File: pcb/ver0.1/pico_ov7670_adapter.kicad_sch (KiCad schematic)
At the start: 19 parts, among them J1 GPIO Header, SW1 SW_Push, SW2 SW_Push, U1 CAMERA-OV7670, U2 RASPBERRY_PI_PICO_W

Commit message: basic rotuing completed
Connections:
- net PICO_IO16: now also J1.10 (Pin_10); no longer J1.4 (Pin_4)
- net PICO_IO17: now also J1.9 (Pin_9); no longer J1.6 (Pin_6)
- net PICO_IO20: now also J1.6 (Pin_6); no longer J1.5 (Pin_5)
- net PICO_IO22: now also J1.4 (Pin_4); no longer J1.8 (Pin_8)
- net USER_Button: now also U2.31 (I2C1_SDA/ADC0/GP26); no longer U2.24 (I2C1_SDA/SPI0_SCK/GP18)
- net USER_LED: now also U2.34 (ADC2_GP28); no longer U2.25 (I2C1_SCL/SPI0_TX/GP19)
- net at R2.2: now also U2.7 (UART1_RX/I2C0_SCL/SPI0_CSN/GP5); no longer U2.16 (UART0_TX/I2C0_SDA/SPI1_RX/GP12)
- net at R6.2: now also U2.6 (UART1_TX/I2C0_SDA/SPI0_RX/GP4); no longer U2.17 (UART0_RX/I2C0_SCL/SPI1_CSN/GP13)
- net PICO_IO21: now reaches U2.27 (12C0_SCL/GP21)
- net PICO_IO21: now also J1.5 (Pin_5)
- net OV_D0_PICO_IO0 renamed OV_D0_PICO_IO14
- net OV_D0_PICO_IO14: now also U2.17 (UART0_RX/I2C0_SCL/SPI1_CSN/GP13); no longer U2.1 (UART0_TX/I2C0_SDA/SPI0_RX/GP0)
- net OV_D1_PICO_IO1 renamed OV_D1_PICO_IO13
- net OV_D1_PICO_IO13: now also U2.16 (UART0_TX/I2C0_SDA/SPI1_RX/GP12); no longer U2.2 (UART0_RX/I2C0_SCL/SPI0_CSN/GP1)
- net OV_D2_PICO_IO2 renamed OV_D2_PICO_IO12
- net OV_D2_PICO_IO12: now also U2.15 (I2C1_SCL/SPI1_TX/GP11); no longer U2.4 (I2C1_SDA/SPI0_SCK/GP2)
- net OV_D3_PICO_IO3 renamed OV_D3_PICO_IO10
- net OV_D3_PICO_IO10: now also U2.14 (I2C1_SDA/SPI1_SCK/GP10); no longer U2.5 (I2C1_SCL/SPI0_TX/GP3)
- net OV_D4_PICO_IO4 renamed OV_D4_PICO_IO9
- net OV_D4_PICO_IO9: now also U2.12 (UART1_RX/I2C0_SCL/SPI1_CSN/GP9); no longer U2.6 (UART1_TX/I2C0_SDA/SPI0_RX/GP4)
- net OV_D5_PICO_IO5 renamed OV_D5_PICO_IO8
- net OV_D5_PICO_IO8: now also U2.11 (UART1_TX/I2C0_SDA/SPI1_RX/GP8); no longer U2.7 (UART1_RX/I2C0_SCL/SPI0_CSN/GP5)
- net OV_D6_PICO_IO6 renamed OV_D6_PICO_IO7
- net OV_D6_PICO_IO7: now also U2.10 (I2C1_SCL/SPI0_TX/GP7); no longer U2.9 (I2C1_SDA/SPI0_SCK/GP6)
- net OV_D7_PICO_IO7 renamed OV_D7_PICO_IO6
- net OV_D7_PICO_IO6: now also U2.9 (I2C1_SDA/SPI0_SCK/GP6); no longer U2.10 (I2C1_SCL/SPI0_TX/GP7)
- net OV_HREF_PICO_IO11 renamed OV_HREF_PICO_IO3
- net OV_HREF_PICO_IO3: now also U2.5 (I2C1_SCL/SPI0_TX/GP3); no longer U2.14 (I2C1_SDA/SPI1_SCK/GP10)
- net OV_PCLK_PICO_IO9 renamed OV_PCLK_PICO_IO4
- net OV_SCL_PICO_IO13_SCL renamed OV_SCL_PICO_IO1_SCL
- net OV_SCL_PICO_IO1_SCL: now also U2.2 (UART0_RX/I2C0_SCL/SPI0_CSN/GP1); no longer U2.12 (UART1_RX/I2C0_SCL/SPI1_CSN/GP9)
- net OV_SDA_PICO_IO12_SDA renamed OV_SDA_PICO_IO0_SDA
- net OV_SDA_PICO_IO0_SDA: now also U2.1 (UART0_TX/I2C0_SDA/SPI0_RX/GP0); no longer U2.11 (UART1_TX/I2C0_SDA/SPI1_RX/GP8)
- net OV_VSYNC_PICO_IO10 renamed OV_VSYNC_PICO_IO2
- net OV_VSYNC_PICO_IO2: now also U2.4 (I2C1_SDA/SPI0_SCK/GP2); no longer U2.15 (I2C1_SCL/SPI1_TX/GP11)
- net OV_XCLK_PICO_IO8 renamed OV_XCLK_PICO_IO5
- net PICO_IO26 renamed PICO_IO19
- net PICO_IO19: now also U2.25 (I2C1_SCL/SPI0_TX/GP19); no longer U2.31 (I2C1_SDA/ADC0/GP26)
- net PICO_IO27: no longer names the net of U2.32 (I2C1_SCL/ADC1/GP27)
- net PICO_IO27: no longer J1.10 (Pin_10)
- removed net PICO_IO28: J1.9 (Pin_9), U2.34 (ADC2_GP28)
- new net PICO_IO18: J1.8 (Pin_8), U2.24 (I2C1_SDA/SPI0_SCK/GP18)
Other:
- moved on the sheet: R2, R6

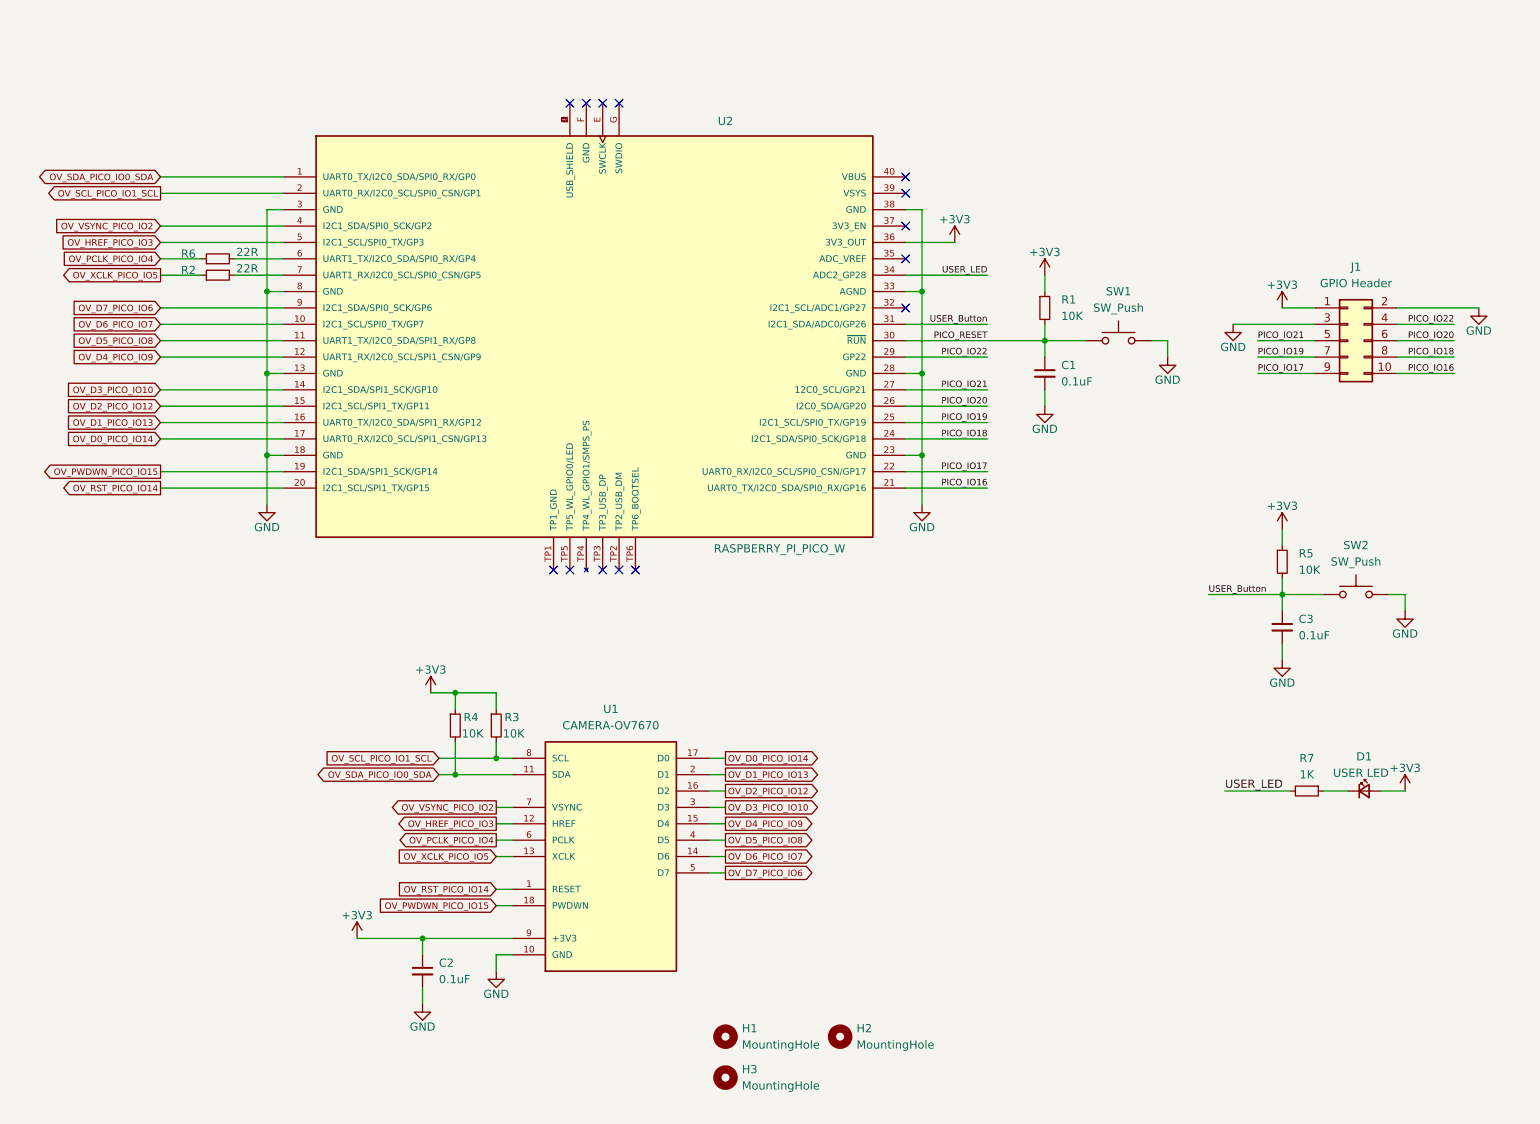
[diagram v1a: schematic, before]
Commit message: GPIO header change updated
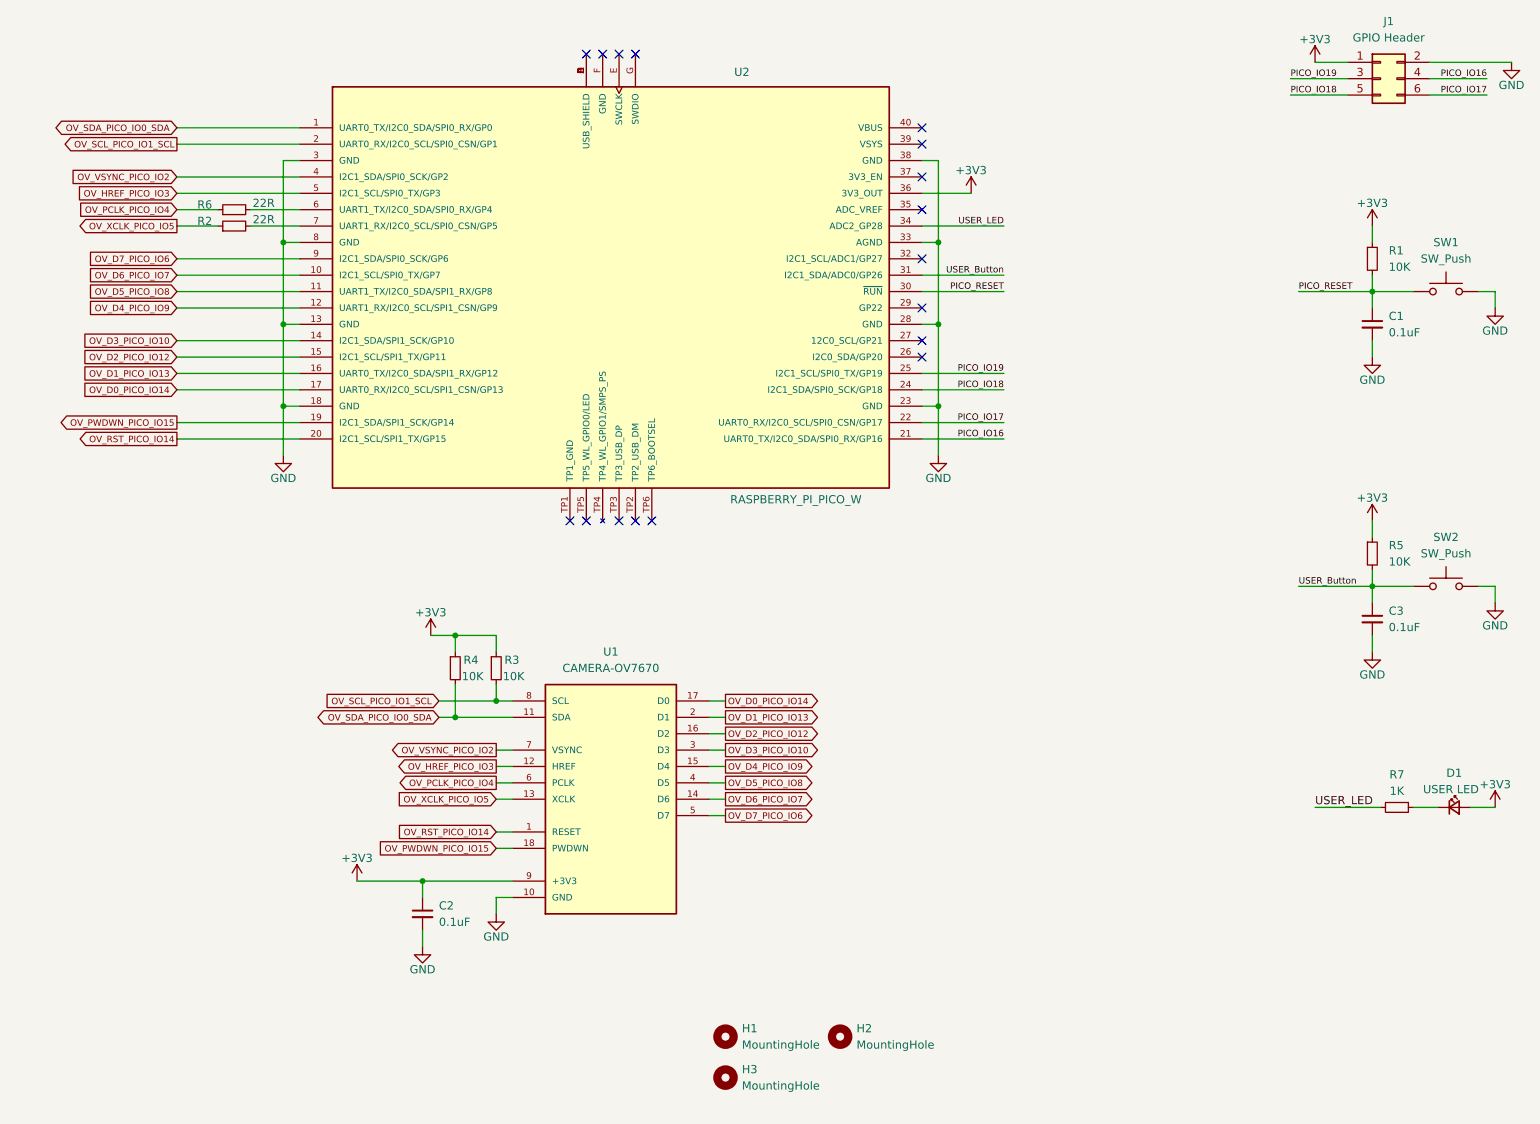
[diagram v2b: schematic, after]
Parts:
- removed J1: GPIO Header, Connector_PinHeader_2.54mm:PinHeader_2x05_P2.54mm_Vertical, symbol Connector_Generic:Conn_02x05_Odd_Even
- added J1: GPIO Header, Connector_PinHeader_2.54mm:PinHeader_2x03_P2.54mm_Vertical, symbol Connector_Generic:Conn_02x03_Odd_Even
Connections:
- net +3V3: now also J1.1 (Pin_1)
- net GND: now also J1.2 (Pin_2)
- net PICO_IO16: now also J1.4 (Pin_4)
- net PICO_IO17: now also J1.6 (Pin_6)
- net PICO_IO18: now also J1.5 (Pin_5)
- net PICO_IO19: now also J1.3 (Pin_3)
- net PICO_IO20: no longer names the net of U2.26 (I2C0_SDA/GP20)
- net PICO_IO21: no longer names the net of U2.27 (12C0_SCL/GP21)
- net PICO_IO22: no longer names the net of U2.29 (GP22)
- no-connect marks 14 -> 17
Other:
- moved on the sheet: C1, C2, C3, D1, R1, R2, R3, R4, R5, R6, R7, SW1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

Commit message: gerber files added
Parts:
- added FID1, FID2, FID3: Fiducial, Fiducial:Fiducial_0.5mm_Mask1mm, symbol Mechanical:Fiducial
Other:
- moved on the sheet: H1, H2, H3
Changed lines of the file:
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@@
 	(symbol
 		(lib_id "Mechanical:MountingHole")
-		(at 139.7 184.15 0)
+		(at 139.7 186.69 0)
 		(unit 1)
 		(exclude_from_sim yes)
@@
 		(fields_autoplaced yes)
 		(property "Reference" "H1"
-			(at 142.24 182.8799 0)
+			(at 142.24 185.4199 0)
 			(effects
 				(font
@@
 		)
 		(property "Value" "MountingHole"
-			(at 142.24 185.4199 0)
+			(at 142.24 187.9599 0)
 			(effects
 				(font
@@
 		)
 		(property "Footprint" "MountingHole:MountingHole_3.2mm_M3_DIN965"
-			(at 139.7 184.15 0)
+			(at 139.7 186.69 0)
 			(effects
 				(font
@@
 		)
 		(property "Datasheet" "~"
-			(at 139.7 184.15 0)
+			(at 139.7 186.69 0)
 			(effects
 				(font
@@
 		)
 		(property "Description" "Mounting Hole without connection"
-			(at 139.7 184.15 0)
+			(at 139.7 186.69 0)
 			(effects
 				(font
@@
 	(symbol
 		(lib_id "Mechanical:MountingHole")
-		(at 139.7 190.5 0)
+		(at 139.7 193.04 0)
 		(unit 1)
 		(exclude_from_sim yes)
@@
 		(fields_autoplaced yes)
 		(property "Reference" "H3"
-			(at 142.24 189.2299 0)
+			(at 142.24 191.7699 0)
 			(effects
 				(font
@@
 		)
 		(property "Value" "MountingHole"
-			(at 142.24 191.7699 0)
+			(at 142.24 194.3099 0)
 			(effects
 				(font
@@
 		)
 		(property "Footprint" "MountingHole:MountingHole_3.2mm_M3_DIN965"
-			(at 139.7 190.5 0)
+			(at 139.7 193.04 0)
 			(effects
 				(font
@@
 		)
 		(property "Datasheet" "~"
-			(at 139.7 190.5 0)
+			(at 139.7 193.04 0)
 			(effects
 				(font
@@
 		)
 		(property "Description" "Mounting Hole without connection"
-			(at 139.7 190.5 0)
+			(at 139.7 193.04 0)
 			(effects
 				(font
@@
 	)
 	(symbol
+		(lib_id "Mechanical:Fiducial")
+		(at 124.46 186.69 0)
+		(unit 1)
+		(exclude_from_sim yes)
+		(in_bom no)
+		(on_board yes)
+		(dnp no)
+		(property "Reference" "FID3"
+			(at 122.174 183.896 0)
+			(effects
+				(font
+					(size 1.27 1.27)
+				)
+				(justify left)
+			)
+		)
+		(property "Value" "Fiducial"
+			(at 127 187.9599 0)
+			(effects
+				(font
+					(size 1.27 1.27)
+				)
+				(justify left)
+				(hide yes)
+			)
+		)
+		(property "Footprint" "Fiducial:Fiducial_0.5mm_Mask1mm"
+			(at 124.46 186.69 0)
+			(effects
+				(font
+					(size 1.27 1.27)
+				)
+				(hide yes)
+			)
+		)
+		(property "Datasheet" "~"
+			(at 124.46 186.69 0)
+			(effects
+				(font
+					(size 1.27 1.27)
+				)
+				(hide yes)
+			)
+		)
+		(property "Description" "Fiducial Marker"
+			(at 124.46 186.69 0)
+			(effects
+				(font
+					(size 1.27 1.27)
+				)
+				(hide yes)
+			)
+		)
+		(instances
+			(project "pico_ov7670_adapter"
+				(path "/8ca4dbff-a6fb-40ff-ba8a-6032e61c2093"
+					(reference "FID3")
+					(unit 1)
+				)
+			)
+		)
+	)
+	(symbol
 		(lib_id "Device:R_Small")
 		(at 240.03 109.22 0)
@@
 	(symbol
 		(lib_id "Mechanical:MountingHole")
-		(at 157.48 184.15 0)
+		(at 157.48 186.69 0)
 		(unit 1)
 		(exclude_from_sim yes)
@@
 		(fields_autoplaced yes)
 		(property "Reference" "H2"
-			(at 160.02 182.8799 0)
+			(at 160.02 185.4199 0)
 			(effects
 				(font
@@
 		)
 		(property "Value" "MountingHole"
-			(at 160.02 185.4199 0)
+			(at 160.02 187.9599 0)
 			(effects
 				(font
@@
 		)
 		(property "Footprint" "MountingHole:MountingHole_3.2mm_M3_DIN965"
-			(at 157.48 184.15 0)
+			(at 157.48 186.69 0)
 			(effects
 				(font
@@
 		)
 		(property "Datasheet" "~"
-			(at 157.48 184.15 0)
+			(at 157.48 186.69 0)
 			(effects
 				(font
@@
 		)
 		(property "Description" "Mounting Hole without connection"
-			(at 157.48 184.15 0)
+			(at 157.48 186.69 0)
 			(effects
 				(font
@@
 	)
 	(symbol
+		(lib_id "Mechanical:Fiducial")
+		(at 116.84 186.69 0)
+		(unit 1)
+		(exclude_from_sim yes)
+		(in_bom no)
+		(on_board yes)
+		(dnp no)
+		(property "Reference" "FID2"
+			(at 114.554 183.896 0)
+			(effects
+				(font
+					(size 1.27 1.27)
+				)
+				(justify left)
+			)
+		)
+		(property "Value" "Fiducial"
+			(at 119.38 187.9599 0)
+			(effects
+				(font
+					(size 1.27 1.27)
+				)
+				(justify left)
+				(hide yes)
+			)
+		)
+		(property "Footprint" "Fiducial:Fiducial_0.5mm_Mask1mm"
+			(at 116.84 186.69 0)
+			(effects
+				(font
+					(size 1.27 1.27)
+				)
+				(hide yes)
+			)
+		)
+		(property "Datasheet" "~"
+			(at 116.84 186.69 0)
+			(effects
+				(font
+					(size 1.27 1.27)
+				)
+				(hide yes)
+			)
+		)
+		(property "Description" "Fiducial Marker"
+			(at 116.84 186.69 0)
+			(effects
+				(font
+					(size 1.27 1.27)
+				)
+				(hide yes)
+			)
+		)
+		(instances
+			(project "pico_ov7670_adapter"
+				(path "/8ca4dbff-a6fb-40ff-ba8a-6032e61c2093"
+					(reference "FID2")
+					(unit 1)
+				)
+			)
+		)
+	)
+	(symbol
 		(lib_id "Switch:SW_Push")
 		(at 251.46 114.3 0)
@@
 					(unit 1)
 				)
+			)
+		)
+	)
+	(symbol
+		(lib_id "Mechanical:Fiducial")
+		(at 109.22 186.69 0)
+		(unit 1)
+		(exclude_from_sim yes)
+		(in_bom no)
+		(on_board yes)
+		(dnp no)
+		(property "Reference" "FID1"
+			(at 106.934 183.896 0)
+			(effects
+				(font
+					(size 1.27 1.27)
+				)
+				(justify left)
+			)
+		)
+		(property "Value" "Fiducial"
+			(at 111.76 187.9599 0)
+			(effects
+				(font
+					(size 1.27 1.27)
+				)
+				(justify left)
+				(hide yes)
+			)
+		)
+		(property "Footprint" "Fiducial:Fiducial_0.5mm_Mask1mm"
+			(at 109.22 186.69 0)
+			(effects
+				(font
+					(size 1.27 1.27)
+				)
+				(hide yes)
+			)
+		)
+		(property "Datasheet" "~"
+			(at 109.22 186.69 0)
+			(effects
+				(font
+					(size 1.27 1.27)
+				)
+				(hide yes)
+			)
+		)
+		(property "Description" "Fiducial Marker"
+			(at 109.22 186.69 0)
+			(effects
+				(font
+					(size 1.27 1.27)
+				)
+				(hide yes)
+			)
+		)
+		(instances
+			(project ""
+				(path "/8ca4dbff-a6fb-40ff-ba8a-6032e61c2093"
+					(reference "FID1")
+					(unit 1)
+				)

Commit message: schematic pdf updated
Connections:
- net OV_D0_PICO_IO14 renamed OV_D0_PICO_IO13
- net OV_D1_PICO_IO13 renamed OV_D1_PICO_IO12
- net OV_D2_PICO_IO12 renamed OV_D2_PICO_IO11
- net OV_PWDWN_PICO_IO15 renamed OV_PWDWN_PICO_IO14
- net OV_RST_PICO_IO14 renamed OV_RST_PICO_IO15
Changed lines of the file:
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@@
 		)
 	)
-	(global_label "OV_D1_PICO_IO13"
+	(global_label "OV_D1_PICO_IO12"
 		(shape input)
 		(at 54.61 81.28 180)
@@
 		)
 	)
-	(global_label "OV_PWDWN_PICO_IO15"
+	(global_label "OV_PWDWN_PICO_IO14"
 		(shape output)
 		(at 54.61 88.9 180)
@@
 		)
 	)
-	(global_label "OV_D0_PICO_IO14"
+	(global_label "OV_D0_PICO_IO13"
 		(shape input)
 		(at 54.61 83.82 180)
@@
 		)
 	)
-	(global_label "OV_D1_PICO_IO13"
+	(global_label "OV_D1_PICO_IO12"
 		(shape output)
 		(at 139.7 134.62 0)
@@
 		)
 	)
-	(global_label "OV_RST_PICO_IO14"
+	(global_label "OV_RST_PICO_IO15"
 		(shape input)
 		(at 104.14 152.4 180)
@@
 		)
 	)
-	(global_label "OV_PWDWN_PICO_IO15"
+	(global_label "OV_PWDWN_PICO_IO14"
 		(shape input)
 		(at 104.14 154.94 180)
@@
 		)
 	)
-	(global_label "OV_D2_PICO_IO12"
+	(global_label "OV_D2_PICO_IO11"
 		(shape input)
 		(at 54.61 78.74 180)
@@
 		)
 	)
-	(global_label "OV_D2_PICO_IO12"
+	(global_label "OV_D2_PICO_IO11"
 		(shape output)
 		(at 139.7 137.16 0)
@@
 		)
 	)
-	(global_label "OV_D0_PICO_IO14"
+	(global_label "OV_D0_PICO_IO13"
 		(shape output)
 		(at 139.7 132.08 0)
@@
 		)
 	)
-	(global_label "OV_RST_PICO_IO14"
+	(global_label "OV_RST_PICO_IO15"
 		(shape output)
 		(at 54.61 91.44 180)
